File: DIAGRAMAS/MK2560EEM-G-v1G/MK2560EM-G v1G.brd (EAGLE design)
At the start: 102.5 x 87.6 mm, 70 parts, among them U1 X-MOTOR, U2 Y-MOTOR, U3 Z-MOTOR

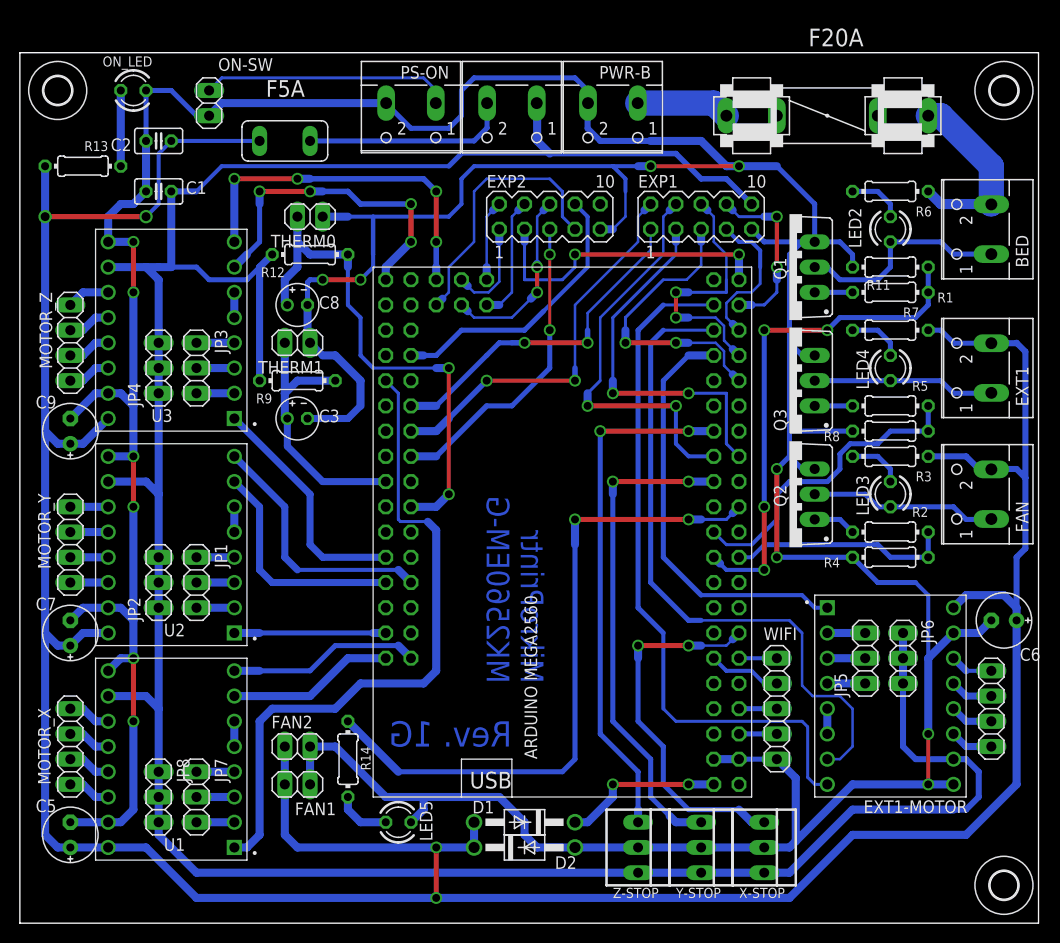
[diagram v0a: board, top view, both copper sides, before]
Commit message: new renders and mods
new 3d rendered pcb images, and also son minor modifications to the pcb layout.
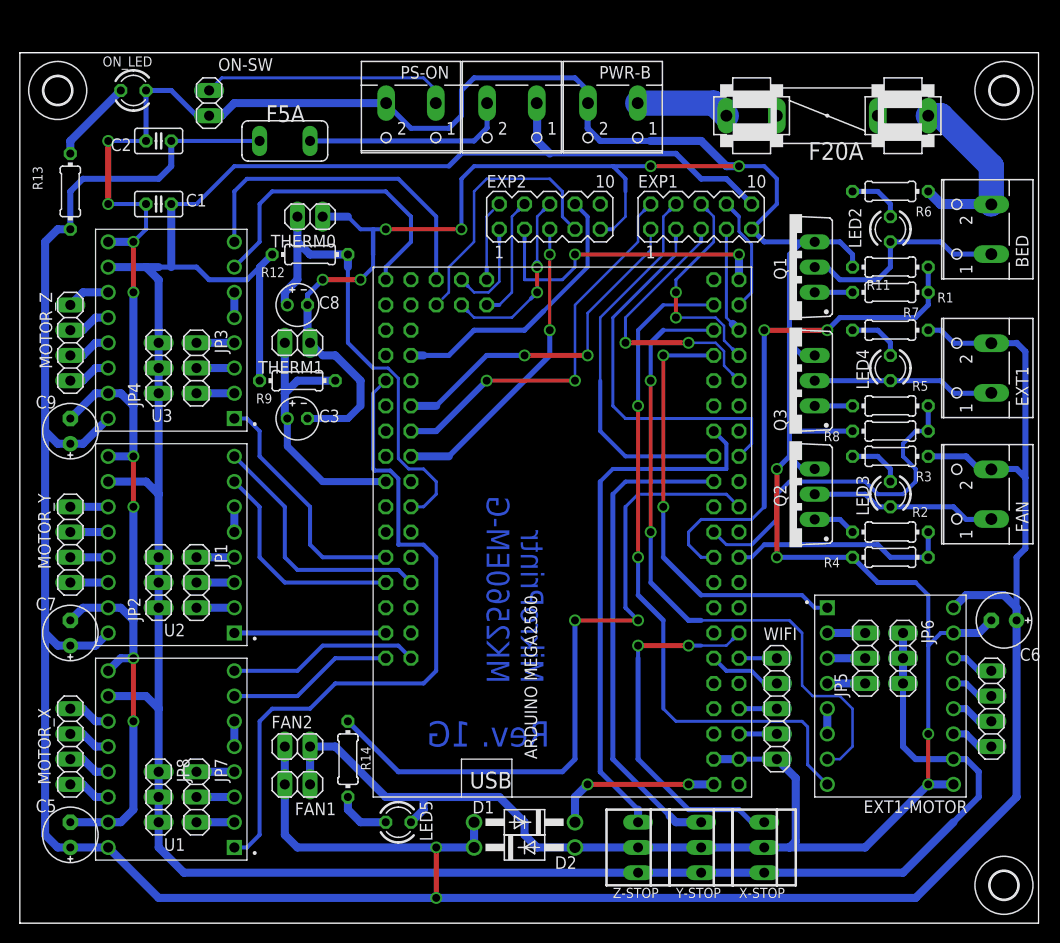
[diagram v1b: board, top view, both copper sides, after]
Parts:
- moved R13 2.84 mm to (2.54, 64.8), turned to 270 degrees
- moved C1 1.27 mm to (11.4, 63.5)
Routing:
- net +12V5A: track 356.2 -> 351.1 mm, vias 4 -> 2
- net D29: track 17.6 -> 12.6 mm, vias 2 -> 0
- net D27: track 15.5 -> 10.7 mm
- net THERM0: track 52.6 -> 48.1 mm, vias 2 -> 0
- net D10: track 31.8 -> 36.0 mm
- net GND: track 507.3 -> 511.5 mm, vias 14 -> 18
- net D25: track 26.3 -> 22.3 mm
- net Z-STEP: track 34.4 -> 31.6 mm, vias 4 -> 0
- net LED: track 67.6 -> 70.2 mm
- net D16: track 41.0 -> 38.5 mm, vias 2 -> 0
- net Z-DIR: track 36.1 -> 33.9 mm, vias 4 -> 0
- net X-EN: track 67.3 -> 69.2 mm
- net D17: track 37.4 -> 39.2 mm, vias 2 -> 0
- net E0-EN: track 42.5 -> 44.0 mm, vias 0 -> 2
- net D23: track 29.8 -> 28.5 mm
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
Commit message: new pcb optimizations
minor pcb error fixes and optimizations.
-changed some thermistors capacitors components for bigger ones.
- added silkscreen pdf for soldering reference.
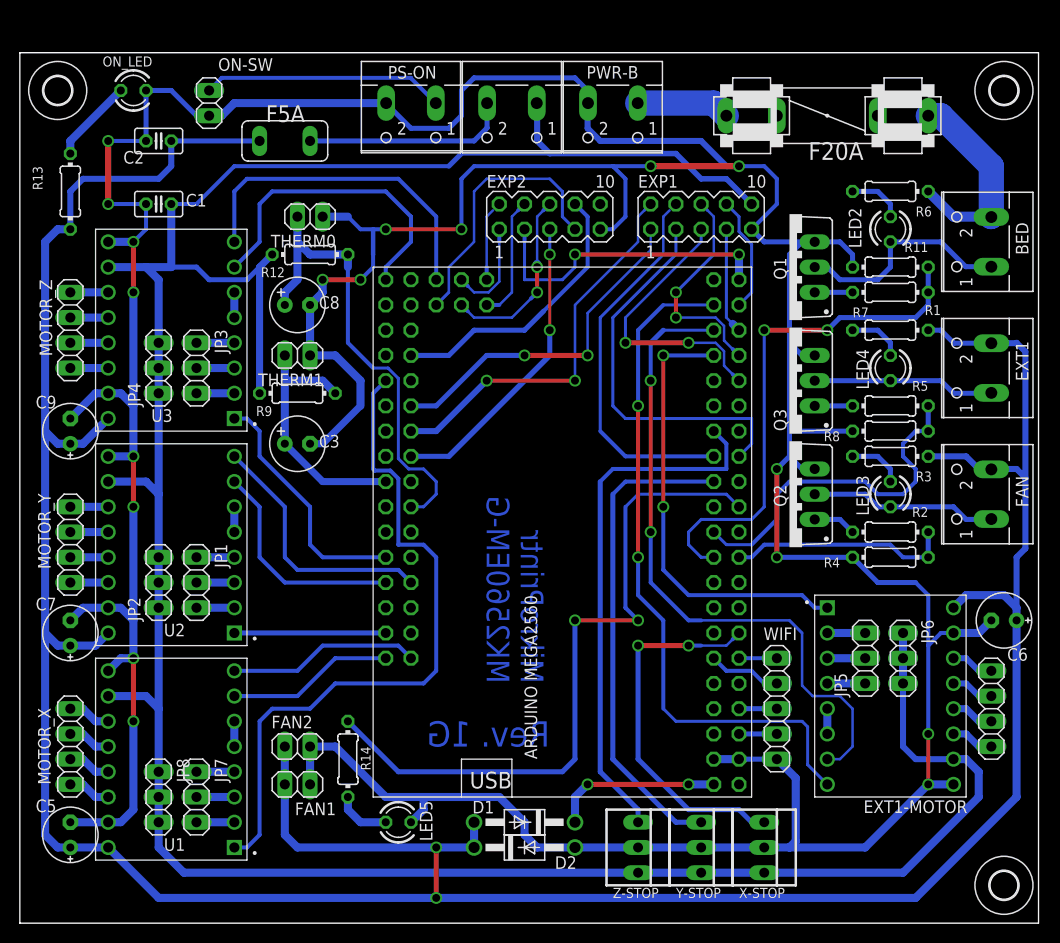
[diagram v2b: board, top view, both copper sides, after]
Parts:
- C3, C8: device rcl:E2-4 -> rcl:E2,5-6
- moved C3 2.54 mm to (25.4, 39.4)
- moved BED 1.27 mm to (94.0, 59.7)
- moved THERM1 1.27 mm to (25.4, 48.3)
- moved MOTOR_Z 1.27 mm to (2.54, 50.8)
- moved R9 1.27 mm to (25.4, 44.5)
- renumbered PWR to +12V_+5V
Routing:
- net +12V: track 19.2 -> 21.0 mm
- net D49: track 26.4 -> 28.2 mm
- net THERM1: track 27.5 -> 26.2 mm
- net +5V: track 294.4 -> 295.6 mm
- net GND: track 511.5 -> 512.7 mm
- net D16: track 38.5 -> 37.6 mm
- net D29: track 12.6 -> 11.7 mm
- net PS_ON: track 25.2 -> 24.4 mm
- net E0-EN: track 44.0 -> 44.8 mm
- net Z-2B: track 4.34 -> 3.81 mm
- net Z-2A: track 4.34 -> 3.81 mm
- net Z-1A: track 4.34 -> 3.81 mm
- net N$7: track 21.9 -> 22.4 mm
- net Z-1B: track 4.34 -> 3.81 mm
